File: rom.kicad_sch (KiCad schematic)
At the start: 2 parts, among them U2 S29GL032N

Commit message: Update schematics for Rev.B:
* Switch obsolete SC16C554BIB48 with SC16C554BIBS
* Change ESP8266 with ESP32-C3
* Add USB-C connector for flashing/debugging
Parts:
- C10: renamed from C2; footprint Capacitors_SMD:C_0805 -> Capacitor_SMD:C_0603_1608Metric; LCSC# C2830722 -> C14663
- U6: renamed from U2; value S29GL032N -> S29GL064N; LCSC# C62389 -> C466861

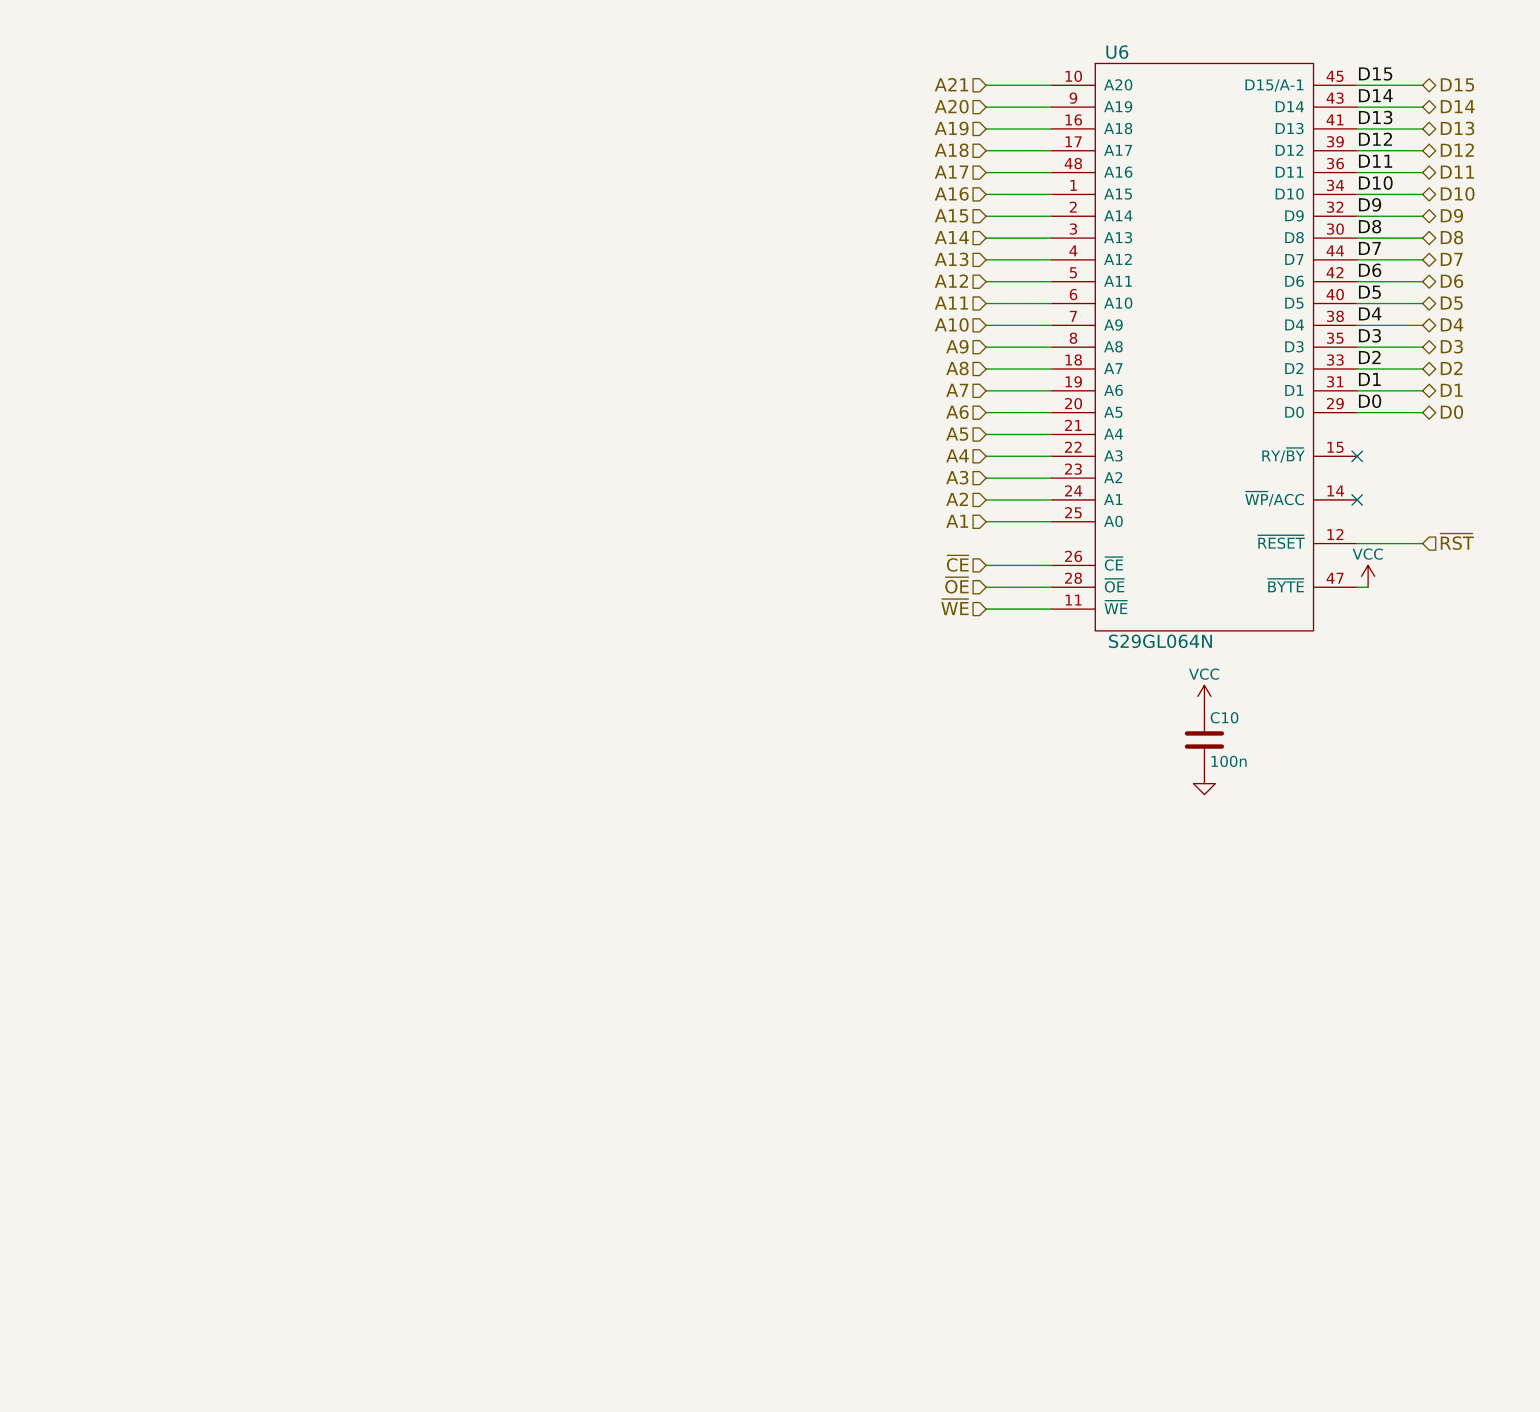
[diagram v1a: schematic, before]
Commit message: Rev.B PCB
* Replace obsolete SC16C550BIB48 with SC16C550BIBS
* Replace ESP8266 with ESP32-C3
* Implement 64 Mbit hack
* Add USB-C debug header for ESP32-C3
* Many PCB improvements
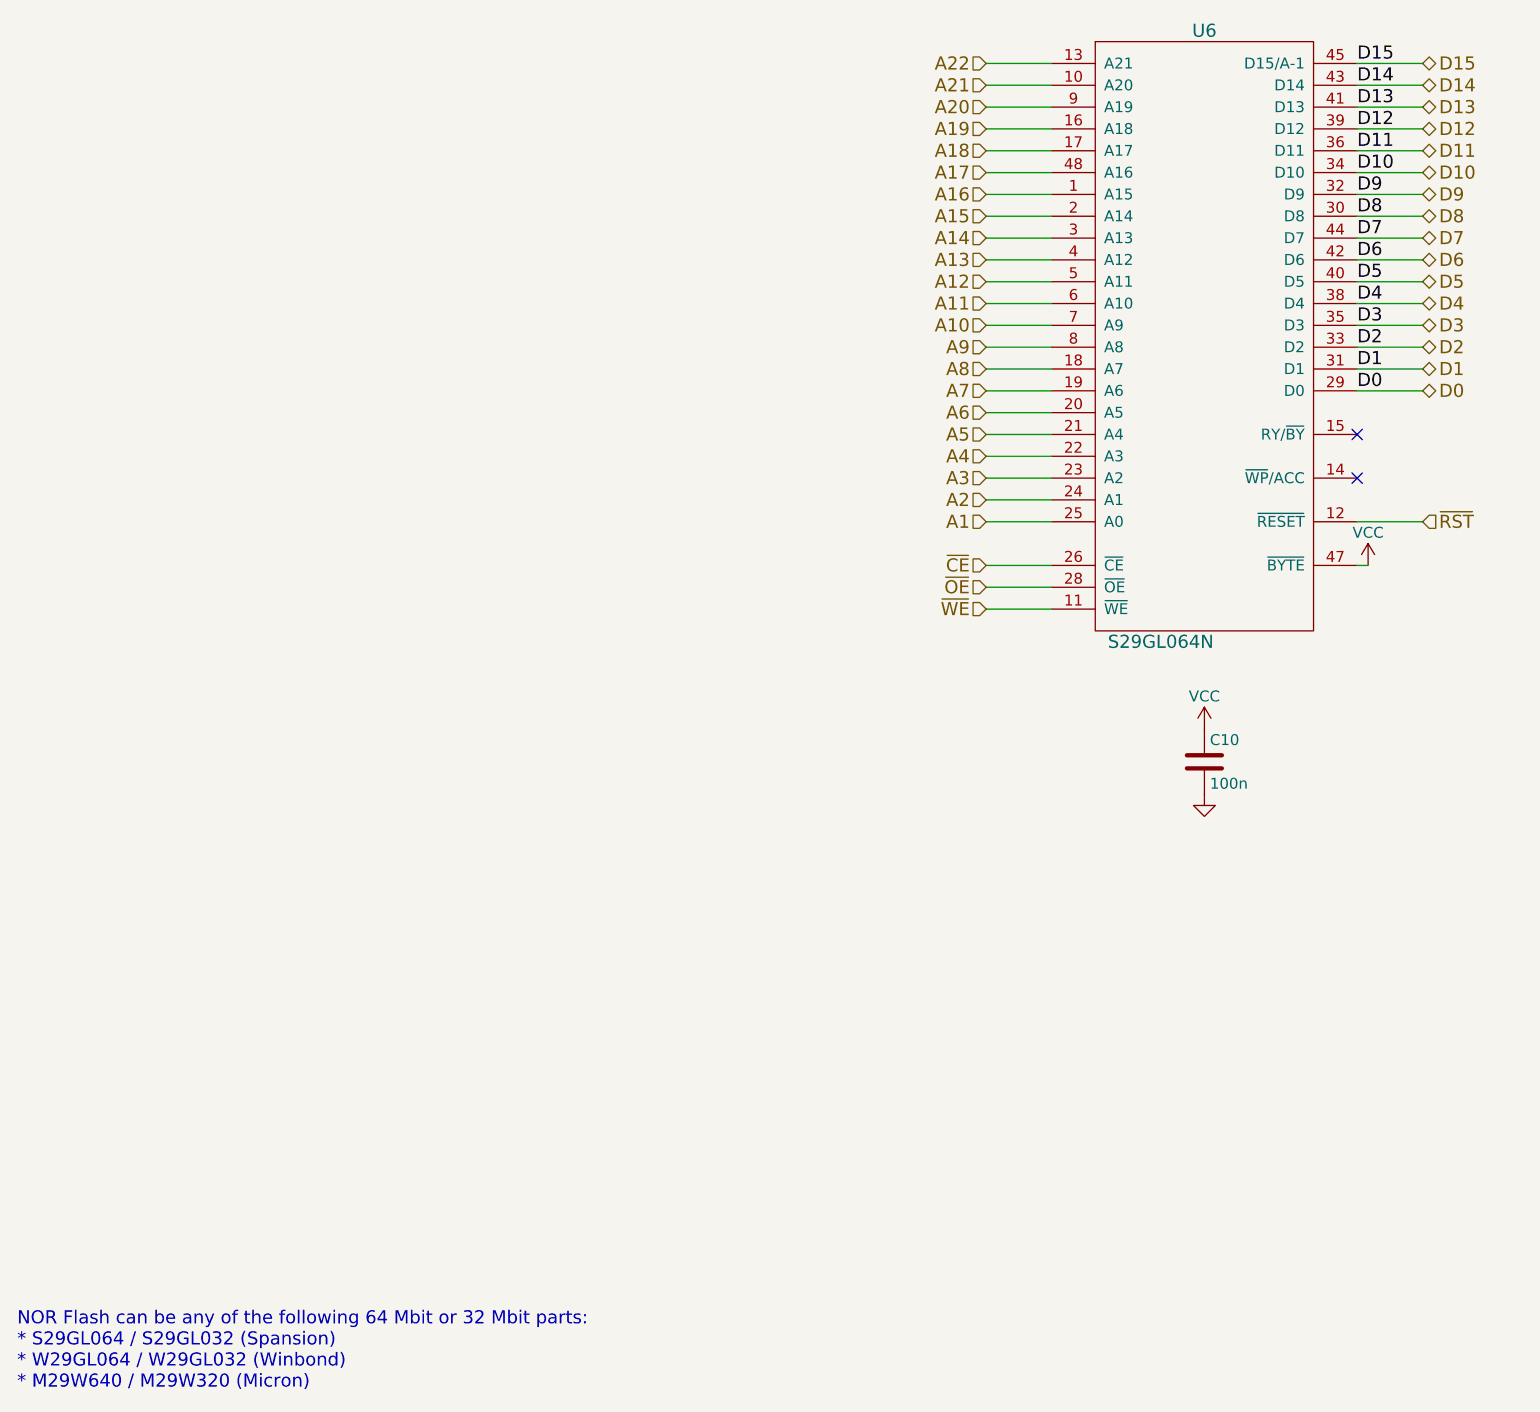
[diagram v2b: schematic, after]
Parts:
- U6: symbol doragasu:S29GL032N -> doragasu:S29GL064N90TFI040; LCSC# C466861 -> C117907
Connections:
- net A22: now reaches U6.13 (A21)
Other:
- note added: "NOR Flash can be any of the following 64 Mbit or 32 Mbit parts: * S29GL064 / S29GL032 (Spansion) * W29GL064 / W29GL032 (Winbond) * M29W640 / M29W320 (Micron)"
- moved on the sheet: C10

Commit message: Fabrication tweaks
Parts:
- U6: footprint doragasu:TSOP48SP -> Package_SO:TSOP-I-48_18.4x12mm_P0.5mm
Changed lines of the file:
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@@
 			)
 		)
-		(property "Footprint" "doragasu:TSOP48SP"
+		(property "Footprint" "Package_SO:TSOP-I-48_18.4x12mm_P0.5mm"
 			(at 156.21 59.69 0)
 			(effects
